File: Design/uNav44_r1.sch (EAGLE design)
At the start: 69 parts, among them IC1 DSPIC33FJ128MC, IC2 24LC024, IC3 AP3417CK-3.3TRG1, IC4 AP6503SP-13, U1 MCP6G01T-E/OT, U2 MCP6G01T-E/OT, U3 MCP6G01T-E/OT, U4 MCP6G01T-E/OT

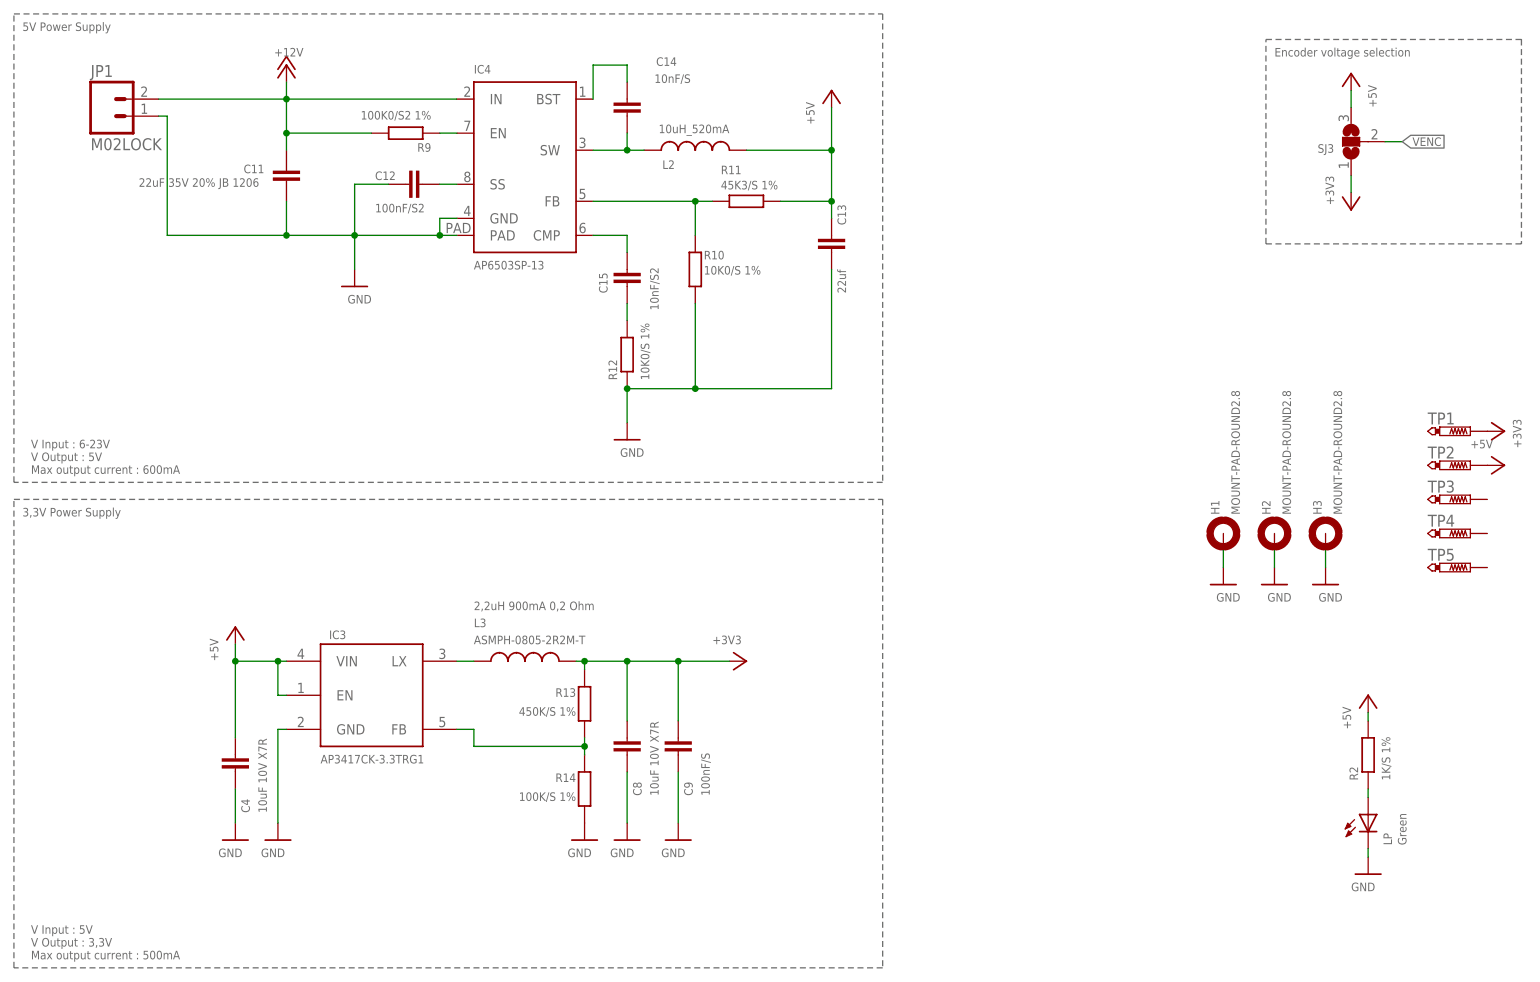
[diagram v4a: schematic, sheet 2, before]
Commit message: Re-Added LDO regulator as option for a LOW-COST version of board. Added jumper to fix IO7 & IO8 to GND to facilitate Encoder cabling in application without Z-Axis
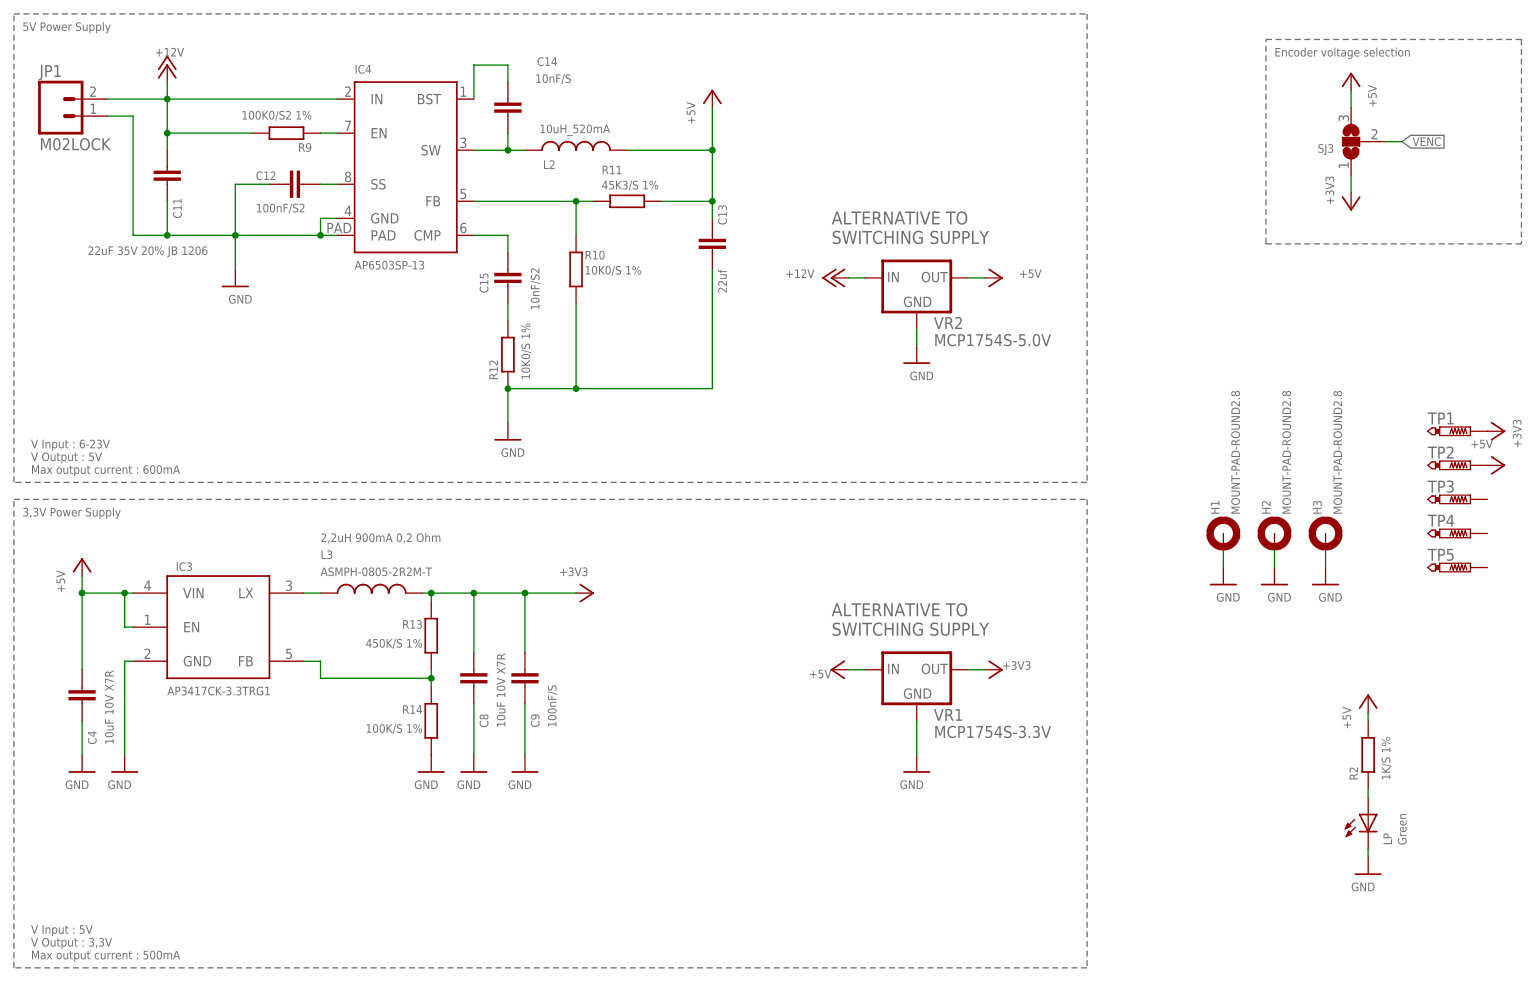
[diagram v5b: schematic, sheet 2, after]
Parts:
- added JMP5, JMP6: 0R-JUMPC, jump-0r-smd:0R-JUMPC
- added VR1: MCP1754S-3.3V, Personale:MCP1754S
- added VR2: MCP1754S-5.0V, Personale:MCP1754S
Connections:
- new net N$10: JMP5-0R.2, SV1.2
- new net N$23: JMP6-0R.2, SV1.1
- net +12V: now also VR2.IN
- net +3V3: now also VR1.OUT
- net +5V: now also VR1.IN, VR2.OUT
- net GND: now also JMP5-0R.3, JMP6-0R.3, VR1.GND, VR2.GND
- net IO7: now also JMP5-0R.1; no longer SV1.2
- net IO8: now also JMP6-0R.1; no longer SV1.1
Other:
- note added: "ALTERNATIVE TO SWITCHING SUPPLY"
- moved on the sheet: C11, C12, C13, C14, C15, C4, C8, C9, IC3, IC4, JP1, L2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

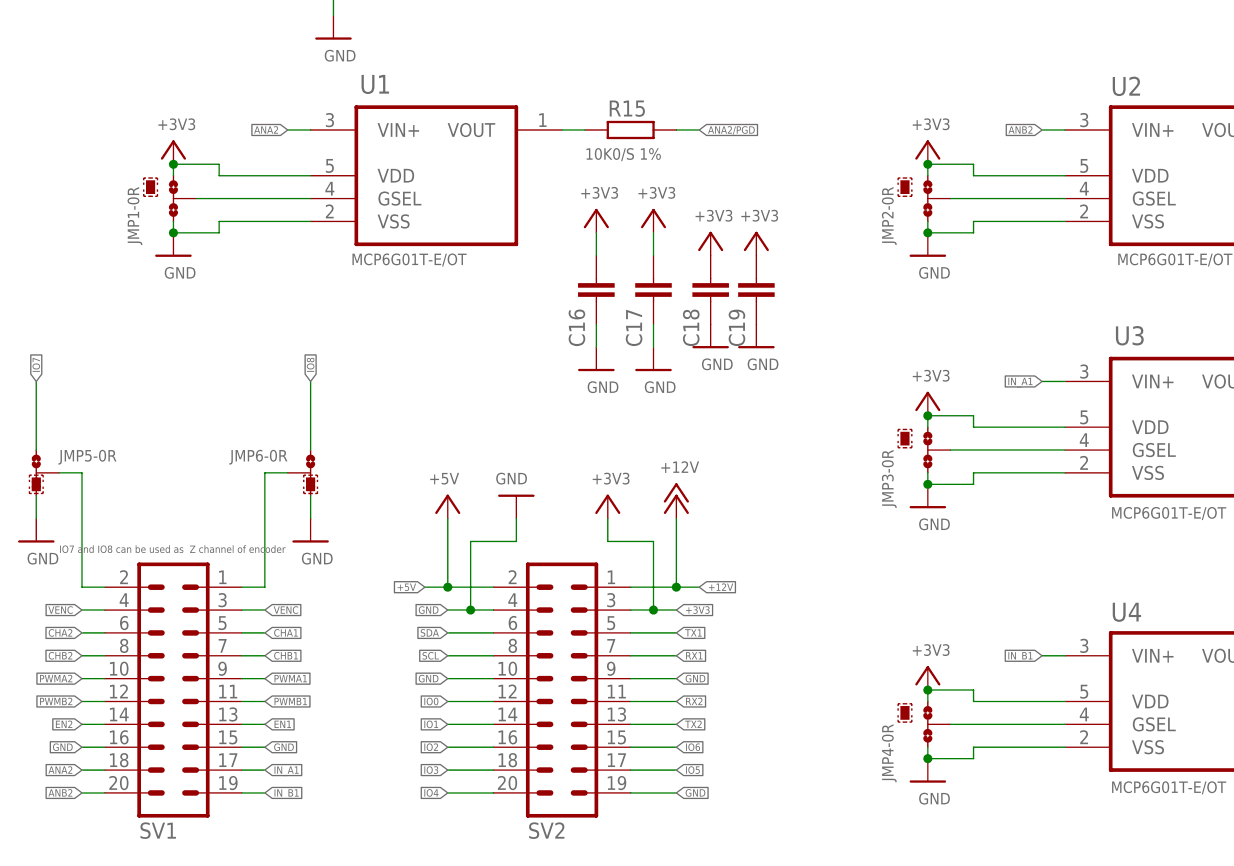
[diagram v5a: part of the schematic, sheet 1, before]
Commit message: With a new 4-via Jumper now OA gain can be controlled by MCU
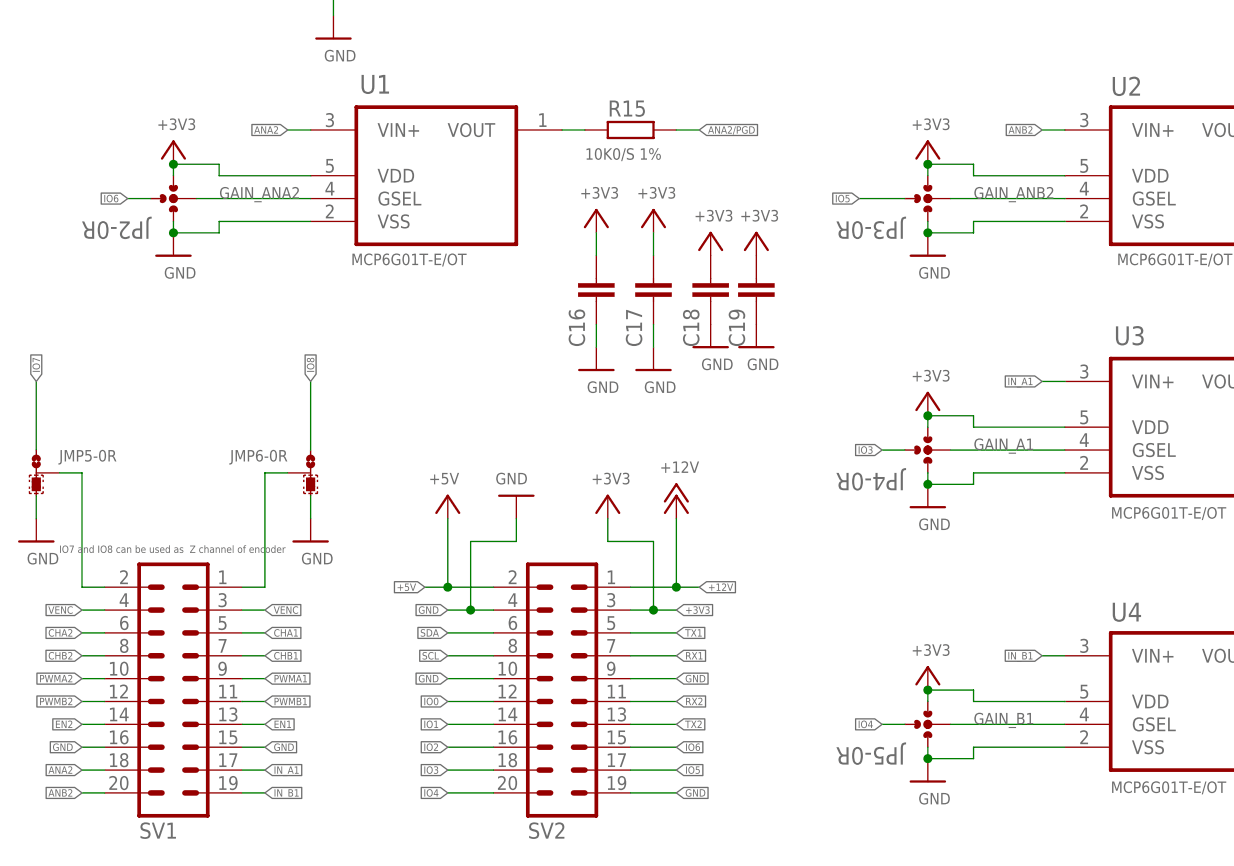
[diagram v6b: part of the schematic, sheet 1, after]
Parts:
- removed JMP1, JMP2, JMP3, JMP4: 0R-JUMPC, jump-0r-smd:0R-JUMPC
- added JP2, JP3, JP4, JP5: (no value), OfficineRobotiche:0R-JUMP-4
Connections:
- removed net N$11: JMP1-0R.2, U1.GSEL
- removed net N$18: JMP2-0R.2, U2.GSEL
- removed net N$19: JMP3-0R.2, U3.GSEL
- removed net N$20: JMP4-0R.2, U4.GSEL
- new net GAIN_A1: JP4-0R.2, U3.GSEL
- new net GAIN_ANA2: JP2-0R.2, U1.GSEL
- new net GAIN_ANB2: JP3-0R.2, U2.GSEL
- new net GAIN_B1: JP5-0R.2, U4.GSEL
- net +3V3: now also JP2-0R.1, JP3-0R.1, JP4-0R.1, JP5-0R.1; no longer JMP1-0R.1, JMP2-0R.1, JMP3-0R.1, JMP4-0R.1
- net GND: now also JP2-0R.3, JP3-0R.3, JP4-0R.3, JP5-0R.3; no longer JMP1-0R.3, JMP2-0R.3, JMP3-0R.3, JMP4-0R.3
- net IO3: now also JP4-0R.4
- net IO4: now also JP5-0R.4
- net IO5: now also JP3-0R.4
- net IO6: now also JP2-0R.4
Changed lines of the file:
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@@
 <part name="GND27" library="supply1" deviceset="GND" device=""/>
 <part name="C4" library="rcl" deviceset="C-EU" device="C0805" value="10uF 10V X7R"/>
-<part name="JMP1" library="jump-0r-smd" deviceset="0R-JUMP" device="C"/>
-<part name="JMP2" library="jump-0r-smd" deviceset="0R-JUMP" device="C"/>
-<part name="JMP3" library="jump-0r-smd" deviceset="0R-JUMP" device="C"/>
-<part name="JMP4" library="jump-0r-smd" deviceset="0R-JUMP" device="C"/>
 <part name="FRAME2" library="frames" deviceset="A4L-LOC" device=""/>
 <part name="H1" library="holes" deviceset="MOUNT-PAD-ROUND" device="2.8"/>
@@
 <part name="GND35" library="supply1" deviceset="GND" device=""/>
 <part name="GND36" library="supply1" deviceset="GND" device=""/>
+<part name="JP2" library="OfficineRobotiche" deviceset="0R-JUMP-4" device=""/>
+<part name="JP3" library="OfficineRobotiche" deviceset="0R-JUMP-4" device=""/>
+<part name="JP4" library="OfficineRobotiche" deviceset="0R-JUMP-4" device=""/>
+<part name="JP5" library="OfficineRobotiche" deviceset="0R-JUMP-4" device=""/>
 </parts>
 <sheets>
@@
 <attribute name="VALUE" x="154.94" y="80.518" size="1.27" layer="96" font="vector"/>
 </instance>
-<instance part="JMP1" gate="-0R" x="25.4" y="76.2" smashed="yes">
-<attribute name="NAME" x="21.59" y="71.12" size="1.27" layer="95" font="vector" rot="R90"/>
-</instance>
-<instance part="JMP1" gate="G$2" x="22.86" y="78.74" smashed="yes"/>
-<instance part="JMP2" gate="-0R" x="109.22" y="76.2" smashed="yes">
-<attribute name="NAME" x="105.41" y="71.12" size="1.27" layer="95" font="vector" rot="R90"/>
-</instance>
-<instance part="JMP2" gate="G$2" x="106.68" y="78.74" smashed="yes"/>
-<instance part="JMP3" gate="-0R" x="109.22" y="48.26" smashed="yes">
-<attribute name="NAME" x="105.41" y="41.91" size="1.27" layer="95" font="vector" rot="R90"/>
-</instance>
-<instance part="JMP3" gate="G$2" x="106.68" y="50.8" smashed="yes"/>
-<instance part="JMP4" gate="-0R" x="109.22" y="17.78" smashed="yes">
-<attribute name="NAME" x="105.41" y="11.43" size="1.27" layer="95" font="vector" rot="R90"/>
-</instance>
-<instance part="JMP4" gate="G$2" x="106.68" y="20.32" smashed="yes"/>
 <instance part="+3V11" gate="G$1" x="72.39" y="74.93" smashed="yes" rot="MR0">
 <attribute name="VALUE" x="74.93" y="76.2" size="1.27" layer="96" font="vector" rot="MR0"/>
@@
 <instance part="GND36" gate="1" x="40.64" y="38.1" smashed="yes">
 <attribute name="VALUE" x="43.18" y="36.83" size="1.27" layer="96" font="vector" rot="R180"/>
+</instance>
+<instance part="JP2" gate="-0R" x="25.4" y="76.2" smashed="yes">
+<attribute name="NAME" x="22.86" y="73.66" size="1.9304" layer="95" ratio="10" rot="SR180"/>
+</instance>
+<instance part="JP3" gate="-0R" x="109.22" y="76.2" smashed="yes">
+<attribute name="NAME" x="106.68" y="73.66" size="1.9304" layer="95" ratio="10" rot="SR180"/>
+</instance>
+<instance part="JP4" gate="-0R" x="109.22" y="48.26" smashed="yes">
+<attribute name="NAME" x="106.68" y="45.72" size="1.9304" layer="95" ratio="10" rot="SR180"/>
+</instance>
+<instance part="JP5" gate="-0R" x="109.22" y="17.78" smashed="yes">
+<attribute name="NAME" x="106.68" y="15.24" size="1.9304" layer="95" ratio="10" rot="SR180"/>
 </instance>
 </instances>
@@
 <pinref part="SV2" gate="G$1" pin="20"/>
 </segment>
+<segment>
+<wire x1="104.14" y1="17.78" x2="106.68" y2="17.78" width="0.1524" layer="91"/>
+<label x="104.14" y="17.78" size="0.8128" layer="95" font="vector" ratio="13" rot="R180" xref="yes"/>
+<pinref part="JP5" gate="-0R" pin="4"/>
+</segment>
 </net>
 <net name="IO3" class="0">
@@
 <pinref part="SV2" gate="G$1" pin="18"/>
 </segment>
+<segment>
+<wire x1="106.68" y1="48.26" x2="104.14" y2="48.26" width="0.1524" layer="91"/>
+<label x="104.14" y="48.26" size="0.8128" layer="95" font="vector" ratio="13" rot="R180" xref="yes"/>
+<pinref part="JP4" gate="-0R" pin="4"/>
+</segment>
 </net>
 <net name="IO2" class="0">
@@
 <pinref part="SV2" gate="G$1" pin="17"/>
 </segment>
+<segment>
+<wire x1="106.68" y1="76.2" x2="101.6" y2="76.2" width="0.1524" layer="91"/>
+<label x="101.6" y="76.2" size="0.8128" layer="95" font="vector" ratio="13" rot="R180" xref="yes"/>
+<pinref part="JP3" gate="-0R" pin="4"/>
+</segment>
 </net>
 <net name="IO6" class="0">
@@
 <label x="81.28" y="15.24" size="0.8128" layer="95" font="vector" rot="MR180" xref="yes"/>
 <pinref part="SV2" gate="G$1" pin="15"/>
+</segment>
+<segment>
+<wire x1="22.86" y1="76.2" x2="20.32" y2="76.2" width="0.1524" layer="91"/>
+<label x="20.32" y="76.2" size="0.8128" layer="95" font="vector" ratio="13" rot="R180" xref="yes"/>
+<pinref part="JP2" gate="-0R" pin="4"/>
 </segment>
 </net>
@@
 <junction x="25.4" y="80.01"/>
 <pinref part="+3V7" gate="G$1" pin="+3V3"/>
-<pinref part="JMP1" gate="-0R" pin="1"/>
 <wire x1="25.4" y1="78.74" x2="25.4" y2="80.01" width="0.1524" layer="91"/>
+<pinref part="JP2" gate="-0R" pin="1"/>
 </segment>
 <segment>
@@
 <junction x="109.22" y="80.01"/>
 <pinref part="+3V8" gate="G$1" pin="+3V3"/>
-<pinref part="JMP2" gate="-0R" pin="1"/>
 <wire x1="109.22" y1="78.74" x2="109.22" y2="80.01" width="0.1524" layer="91"/>
+<pinref part="JP3" gate="-0R" pin="1"/>
 </segment>
 <segment>
@@
 <junction x="109.22" y="52.07"/>
 <pinref part="+3V9" gate="G$1" pin="+3V3"/>
-<pinref part="JMP3" gate="-0R" pin="1"/>
 <wire x1="109.22" y1="50.8" x2="109.22" y2="52.07" width="0.1524" layer="91"/>
+<pinref part="JP4" gate="-0R" pin="1"/>
 </segment>
 <segment>
@@
 <junction x="109.22" y="21.59"/>
 <pinref part="+3V10" gate="G$1" pin="+3V3"/>
-<pinref part="JMP4" gate="-0R" pin="1"/>
 <wire x1="109.22" y1="20.32" x2="109.22" y2="21.59" width="0.1524" layer="91"/>
+<pinref part="JP5" gate="-0R" pin="1"/>
 </segment>
 <segment>
@@
 <junction x="25.4" y="72.39"/>
 <pinref part="GND28" gate="1" pin="GND"/>
-<pinref part="JMP1" gate="-0R" pin="3"/>
 <wire x1="25.4" y1="73.66" x2="25.4" y2="72.39" width="0.1524" layer="91"/>
+<pinref part="JP2" gate="-0R" pin="3"/>
 </segment>
 <segment>
@@
 <junction x="109.22" y="72.39"/>
 <pinref part="GND29" gate="1" pin="GND"/>
-<pinref part="JMP2" gate="-0R" pin="3"/>
 <wire x1="109.22" y1="73.66" x2="109.22" y2="72.39" width="0.1524" layer="91"/>
+<pinref part="JP3" gate="-0R" pin="3"/>
 </segment>
 <segment>
@@
 <junction x="109.22" y="44.45"/>
 <pinref part="GND30" gate="1" pin="GND"/>
-<pinref part="JMP3" gate="-0R" pin="3"/>
 <wire x1="109.22" y1="45.72" x2="109.22" y2="44.45" width="0.1524" layer="91"/>
+<pinref part="JP4" gate="-0R" pin="3"/>
 </segment>
 <segment>
@@
 <junction x="109.22" y="13.97"/>
 <pinref part="GND31" gate="1" pin="GND"/>
-<pinref part="JMP4" gate="-0R" pin="3"/>
 <wire x1="109.22" y1="15.24" x2="109.22" y2="13.97" width="0.1524" layer="91"/>
+<pinref part="JP5" gate="-0R" pin="3"/>
 </segment>
 <segment>
@@
 </segment>
 </net>
-<net name="N$11" class="0">
+<net name="GAIN_ANA2" class="0">
 <segment>
 <pinref part="U1" gate="A" pin="GSEL"/>
 <wire x1="27.94" y1="76.2" x2="40.64" y2="76.2" width="0.1524" layer="91"/>
-<pinref part="JMP1" gate="-0R" pin="2"/>
-</segment>
-</net>
-<net name="N$18" class="0">
+<label x="30.48" y="76.2" size="1.27" layer="95" font="vector" ratio="15"/>
+<pinref part="JP2" gate="-0R" pin="2"/>
+</segment>
+</net>
+<net name="GAIN_ANB2" class="0">
 <segment>
 <pinref part="U2" gate="A" pin="GSEL"/>
 <wire x1="111.76" y1="76.2" x2="124.46" y2="76.2" width="0.1524" layer="91"/>
-<pinref part="JMP2" gate="-0R" pin="2"/>
-</segment>
-</net>
-<net name="N$19" class="0">
+<label x="114.3" y="76.2" size="1.27" layer="95" font="vector" ratio="15"/>
+<pinref part="JP3" gate="-0R" pin="2"/>
+</segment>
+</net>
+<net name="GAIN_A1" class="0">
 <segment>
 <pinref part="U3" gate="A" pin="GSEL"/>
 <wire x1="111.76" y1="48.26" x2="124.46" y2="48.26" width="0.1524" layer="91"/>
-<pinref part="JMP3" gate="-0R" pin="2"/>
-</segment>
-</net>
-<net name="N$20" class="0">
+<label x="114.3" y="48.26" size="1.27" layer="95" font="vector" ratio="15"/>
+<pinref part="JP4" gate="-0R" pin="2"/>
+</segment>
+</net>
+<net name="GAIN_B1" class="0">
 <segment>
 <pinref part="U4" gate="A" pin="GSEL"/>
 <wire x1="111.76" y1="17.78" x2="124.46" y2="17.78" width="0.1524" layer="91"/>
-<pinref part="JMP4" gate="-0R" pin="2"/>
-</segment>
-</net>
+<label x="114.3" y="17.78" size="1.27" layer="95" font="vector" ratio="15"/>
+<pinref part="JP5" gate="-0R" pin="2"/>
+</segment>
+</net>
